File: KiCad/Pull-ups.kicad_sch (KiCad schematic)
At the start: 21 parts

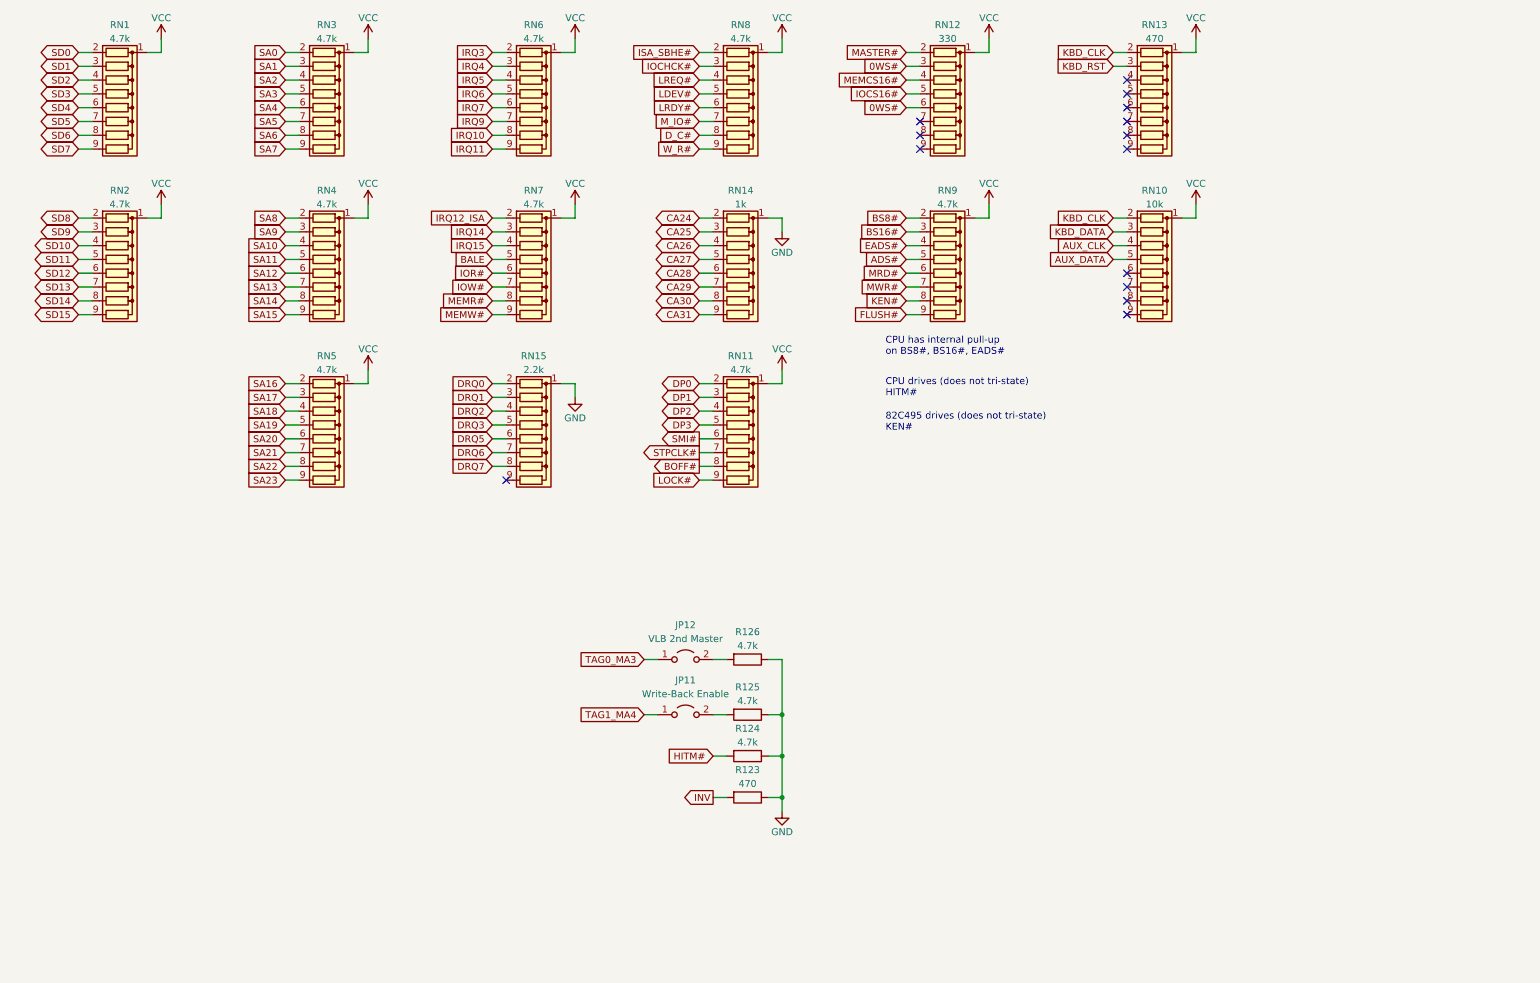
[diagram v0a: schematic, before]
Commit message: Version 0.3: Update DRAM schematic, pull-ups/pull-downs, CPU configuration jumpers
Signed-off-by: Sergey Kiselev <skiselev@gmail.com>
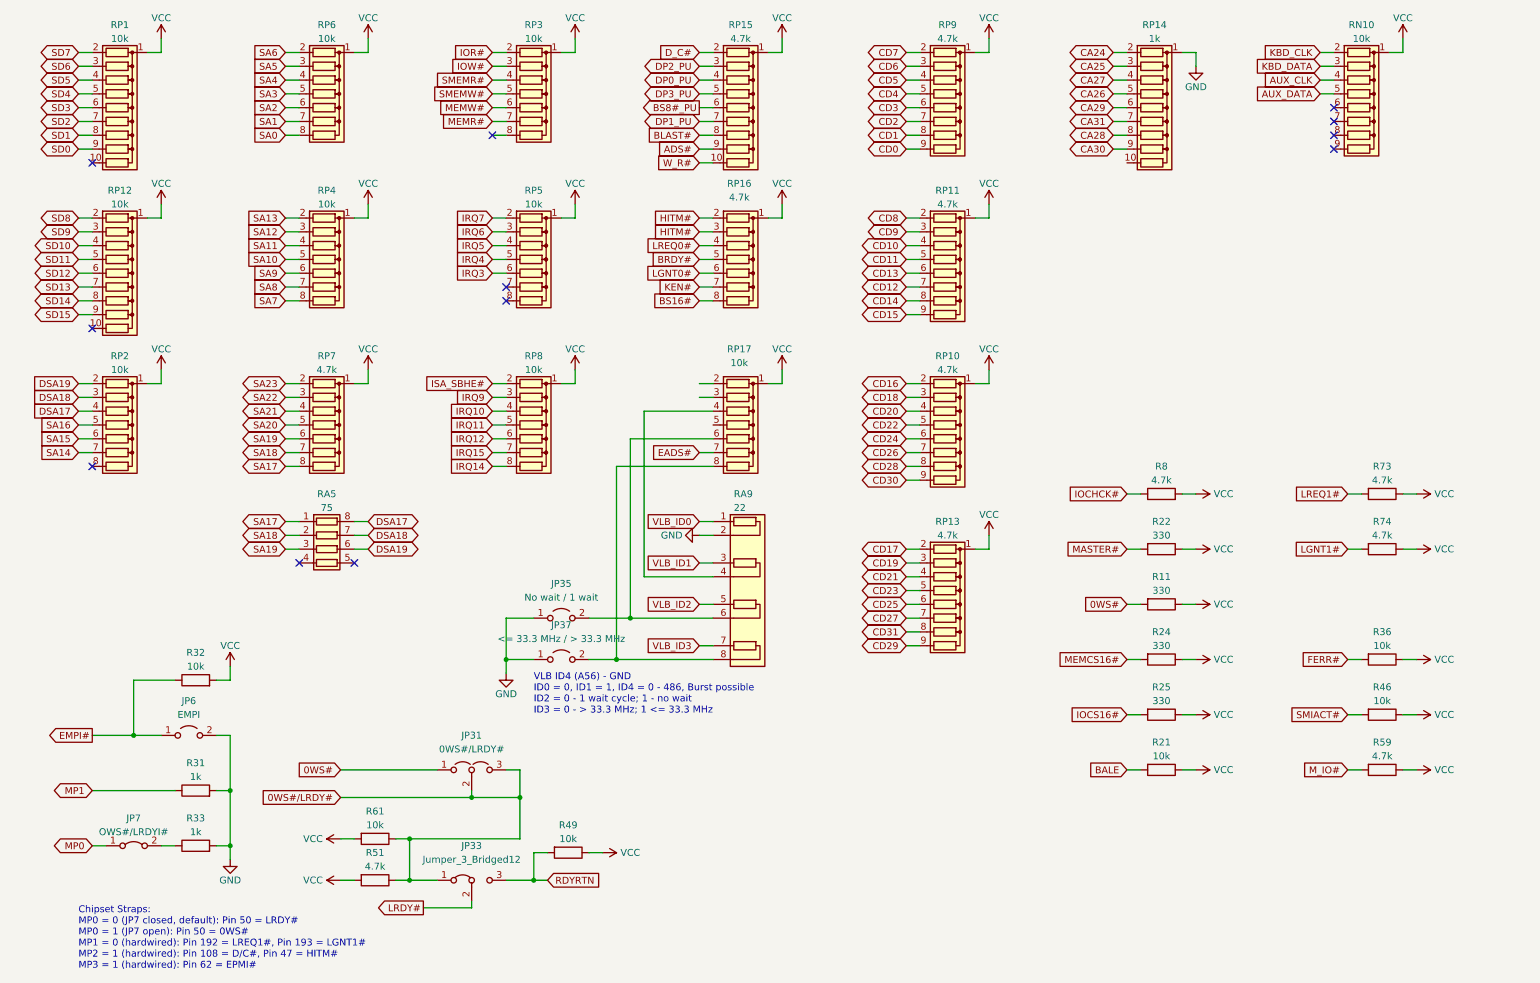
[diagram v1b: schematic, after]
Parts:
- removed JP11: Write-Back Enable, symbol Jumper:Jumper_2_Open
- removed JP12: VLB 2nd Master, symbol Jumper:Jumper_2_Open
- removed R123: 470, symbol Device:R
- removed R124, R125, R126: 4.7k, symbol Device:R
- removed RN1, RN11, RN2, RN3, RN4, RN5, RN6, RN7, RN8, RN9: 4.7k, Resistor_THT:R_Array_SIP9, symbol Device:R_Network08
- removed RN12: 330, Resistor_THT:R_Array_SIP9, symbol Device:R_Network08
- removed RN13: 470, Resistor_THT:R_Array_SIP9, symbol Device:R_Network08
- removed RN14: 1k, Resistor_THT:R_Array_SIP9, symbol Device:R_Network08
- removed RN15: 2.2k, Resistor_THT:R_Array_SIP9, symbol Device:R_Network08
- added JP31: 0WS#/LRDY#, symbol Jumper:Jumper_3_Open
- added JP33: Jumper_3_Bridged12, symbol Jumper:Jumper_3_Bridged12
- added JP35: No wait / 1 wait, symbol Jumper:Jumper_2_Open
- added JP37: <= 33.3 MHz / > 33.3 MHz, symbol Jumper:Jumper_2_Open
- added JP6: EMPI, symbol Jumper:Jumper_2_Open
- added JP7: OWS#/LRDYI#, symbol Jumper:Jumper_2_Bridged
- added R11, R22, R24, R25: 330, symbol Device:R
- added R21, R32, R36, R46, R49, R61: 10k, symbol Device:R
- added R31, R33: 1k, symbol Device:R
- added R51, R59, R73, R74, R8: 4.7k, symbol Device:R
- added RA5: 75, symbol Device:R_Pack04
- added RA9: 22, Resistor_THT:R_Array_SIP8, symbol Device:R_Pack04_SIP
- added RP1, RP12: 10k, Resistor_THT:R_Array_SIP10, symbol Device:R_Network09
- added RP10, RP11, RP13, RP9: 4.7k, Resistor_THT:R_Array_SIP9, symbol Device:R_Network08
- added RP14: 1k, Resistor_THT:R_Array_SIP10, symbol Device:R_Network09
- added RP15: 4.7k, Resistor_THT:R_Array_SIP10, symbol Device:R_Network09
- added RP16, RP7: 4.7k, Resistor_THT:R_Array_SIP8, symbol Device:R_Network07
- added RP17, RP2, RP3, RP4, RP5, RP6, RP8: 10k, Resistor_THT:R_Array_SIP8, symbol Device:R_Network07
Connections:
- net 0WS#: now also JP31.1 (A), R11.2
- net ADS#: now also RP15.9 (R8)
- net BALE: now also R21.2
- net BS16#: now also RP16.8 (R7)
- net CA24: now also RP14.2 (R1)
- net CA25: now also RP14.3 (R2)
- net CA26: now also RP14.5 (R4)
- net CA27: now also RP14.4 (R3)
- net CA28: now also RP14.8 (R7)
- net CA29: now also RP14.6 (R5)
- net CA30: now also RP14.9 (R8)
- net CA31: now also RP14.7 (R6)
- net D_C#: now also RP15.2 (R1)
- net EADS#: now also RP17.7 (R6)
- net GND: now also JP35.1 (A), JP37.1 (A), JP6.2 (B), R31.2, R33.2, RA9.2 (R1.2), RP14.1 (common)
- net HITM#: now also RP16.2 (R1), RP16.3 (R2)
- net IOCHCK#: now also R8.1
- net IOCS16#: now also R25.2
- net IOR#: now also RP3.2 (R1)
- net IOW#: now also RP3.3 (R2)
- net IRQ10: now also RP8.4 (R3)
- net IRQ11: now also RP8.5 (R4)
- net IRQ14: now also RP8.8 (R7)
- net IRQ15: now also RP8.7 (R6)
- net IRQ3: now also RP5.6 (R5)
- net IRQ4: now also RP5.5 (R4)
- net IRQ5: now also RP5.4 (R3)
- net IRQ6: now also RP5.3 (R2)
- net IRQ7: now also RP5.2 (R1)
- net IRQ9: now also RP8.3 (R2)
- net ISA_SBHE#: now also RP8.2 (R1)
- net KEN#: now also RP16.7 (R6)
- net LRDY#: now also JP33.2 (C)
- net MASTER#: now also R22.2
- net MEMCS16#: now also R24.2
- net MEMR#: now also RP3.7 (R6)
- net MEMW#: now also RP3.6 (R5)
- net M_IO#: now also R59.2
- net SA0: now also RP6.8 (R7)
- net SA1: now also RP6.7 (R6)
- net SA10: now also RP4.5 (R4)
- net SA11: now also RP4.4 (R3)
- net SA12: now also RP4.3 (R2)
- net SA13: now also RP4.2 (R1)
- net SA14: now also RP2.7 (R6)
- net SA15: now also RP2.6 (R5)
- net SA16: now also RP2.5 (R4)
- net SA17: now also RA5.1 (R1.1), RP7.8 (R7)
- net SA18: now also RA5.2 (R2.1), RP7.7 (R6)
- net SA19: now also RA5.3 (R3.1), RP7.6 (R5)
- net SA2: now also RP6.6 (R5)
- net SA20: now also RP7.5 (R4)
- net SA21: now also RP7.4 (R3)
- net SA22: now also RP7.3 (R2)
- net SA23: now also RP7.2 (R1)
- net SA3: now also RP6.5 (R4)
- net SA4: now also RP6.4 (R3)
- net SA5: now also RP6.3 (R2)
- net SA6: now also RP6.2 (R1)
- net SA7: now also RP4.8 (R7)
- net SA8: now also RP4.7 (R6)
- net SA9: now also RP4.6 (R5)
- net SD0: now also RP1.9 (R8)
- net SD1: now also RP1.8 (R7)
- net SD10: now also RP12.4 (R3)
- net SD11: now also RP12.5 (R4)
- net SD12: now also RP12.6 (R5)
- net SD13: now also RP12.7 (R6)
- net SD14: now also RP12.8 (R7)
- net SD15: now also RP12.9 (R8)
- net SD2: now also RP1.7 (R6)
- net SD3: now also RP1.6 (R5)
- net SD4: now also RP1.5 (R4)
- net SD5: now also RP1.4 (R3)
- net SD6: now also RP1.3 (R2)
- net SD7: now also RP1.2 (R1)
- net SD8: now also RP12.2 (R1)
- net SD9: now also RP12.3 (R2)
- net VCC: now also R11.1, R21.1, R22.1, R24.1, R25.1, R32.2, R36.1, R46.1, R49.1, R51.2, R59.1, R61.2, R73.1, R74.1, R8.2, RP1.1 (common), RP10.1 (common), RP11.1 (common), RP12.1 (common), RP13.1 (common), RP15.1 (common), RP16.1 (common), RP17.1 (common), RP2.1 (common), RP3.1 (common), RP4.1 (common), RP5.1 (common), RP6.1 (common), RP7.1 (common), RP8.1 (common), RP9.1 (common)
- net W_R#: now also RP15.10 (R9)
- new net: RA9.4 (R2.2), RP17.4 (R3)
- new net: JP35.2 (B), RA9.6 (R3.2), RP17.6 (R5)
- new net: JP37.2 (B), RA9.8 (R4.2), RP17.8 (R7)
- new net: JP7.2 (B), R33.1
- new net 0WS#/LRDY#: JP31.2 (C), JP31.3 (B), JP33.1 (A), R51.1, R61.1
- new net BLAST#: RP15.8 (R7)
- new net BRDY#: RP16.5 (R4)
- new net BS8#_PU: RP15.6 (R5)
- new net CD0: RP9.9 (R8)
- new net CD1: RP9.8 (R7)
- new net CD10: RP11.4 (R3)
- new net CD11: RP11.5 (R4)
- new net CD12: RP11.7 (R6)
- new net CD13: RP11.6 (R5)
- new net CD14: RP11.8 (R7)
- new net CD15: RP11.9 (R8)
- new net CD16: RP10.2 (R1)
- new net CD17: RP13.2 (R1)
- new net CD18: RP10.3 (R2)
- new net CD19: RP13.3 (R2)
- new net CD2: RP9.7 (R6)
- new net CD20: RP10.4 (R3)
- new net CD21: RP13.4 (R3)
- new net CD22: RP10.5 (R4)
- new net CD23: RP13.5 (R4)
- new net CD24: RP10.6 (R5)
- new net CD25: RP13.6 (R5)
- new net CD26: RP10.7 (R6)
- new net CD27: RP13.7 (R6)
- new net CD28: RP10.8 (R7)
- new net CD29: RP13.9 (R8)
- new net CD3: RP9.6 (R5)
- new net CD30: RP10.9 (R8)
- new net CD31: RP13.8 (R7)
- new net CD4: RP9.5 (R4)
- new net CD5: RP9.4 (R3)
- new net CD6: RP9.3 (R2)
- new net CD7: RP9.2 (R1)
- new net CD8: RP11.2 (R1)
- new net CD9: RP11.3 (R2)
- new net DP0_PU: RP15.4 (R3)
- new net DP1_PU: RP15.7 (R6)
- new net DP2_PU: RP15.3 (R2)
- new net DP3_PU: RP15.5 (R4)
- new net DSA17: RA5.8 (R1.2), RP2.4 (R3)
- new net DSA18: RA5.7 (R2.2), RP2.3 (R2)
- new net DSA19: RA5.6 (R3.2), RP2.2 (R1)
- new net EMPI#: JP6.1 (A), R32.1
- new net FERR#: R36.2
- new net IRQ12: RP8.6 (R5)
- new net LGNT0#: RP16.6 (R5)
- new net LGNT1#: R74.2
- new net LREQ0#: RP16.4 (R3)
- new net LREQ1#: R73.2
- new net MP0: JP7.1 (A)
- new net MP1: R31.1
- new net RDYRTN: JP33.3 (B), R49.2
- new net SMEMR#: RP3.4 (R3)
- new net SMEMW#: RP3.5 (R4)
- new net SMIACT#: R46.2
- new net VLB_ID0: RA9.1 (R1.1)
- new net VLB_ID1: RA9.3 (R2.1)
- new net VLB_ID2: RA9.5 (R3.1)
- new net VLB_ID3: RA9.7 (R4.1)
- no-connect marks 14 -> 12
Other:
- note added: "Chipset Straps: MP0 = 0 (JP7 closed, default): Pin 50 = LRDY# MP0 = 1 (JP7 open): Pin 50 = 0WS# MP1 = 0 (hardwired): Pin 192 = LREQ1#, Pin 193 = LGNT1# MP2 = 1 (hardwired): Pin 108 = D/C#, Pin 47 = HITM# MP3 = 1 (hardwired): Pin 62 = EPMI#"
- note added: "VLB ID4 (A56) - GND ID0 = 0, ID1 = 1, ID4 = 0 - 486, Burst possible ID2 = 0 - 1 wait cycle; 1 - no wait ID3 = 0 - > 33.3 MHz; 1 <= 33.3 MHz"
- note removed: "82C495 drives (does not tri-state) KEN#"
- note removed: "CPU drives (does not tri-state) HITM#"
- note removed: "CPU has internal pull-up on BS8#, BS16#, EADS#"
- moved on the sheet: RN10

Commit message: Version 0.4: Update chipset connection
Signed-off-by: Sergey Kiselev <skiselev@gmail.com>
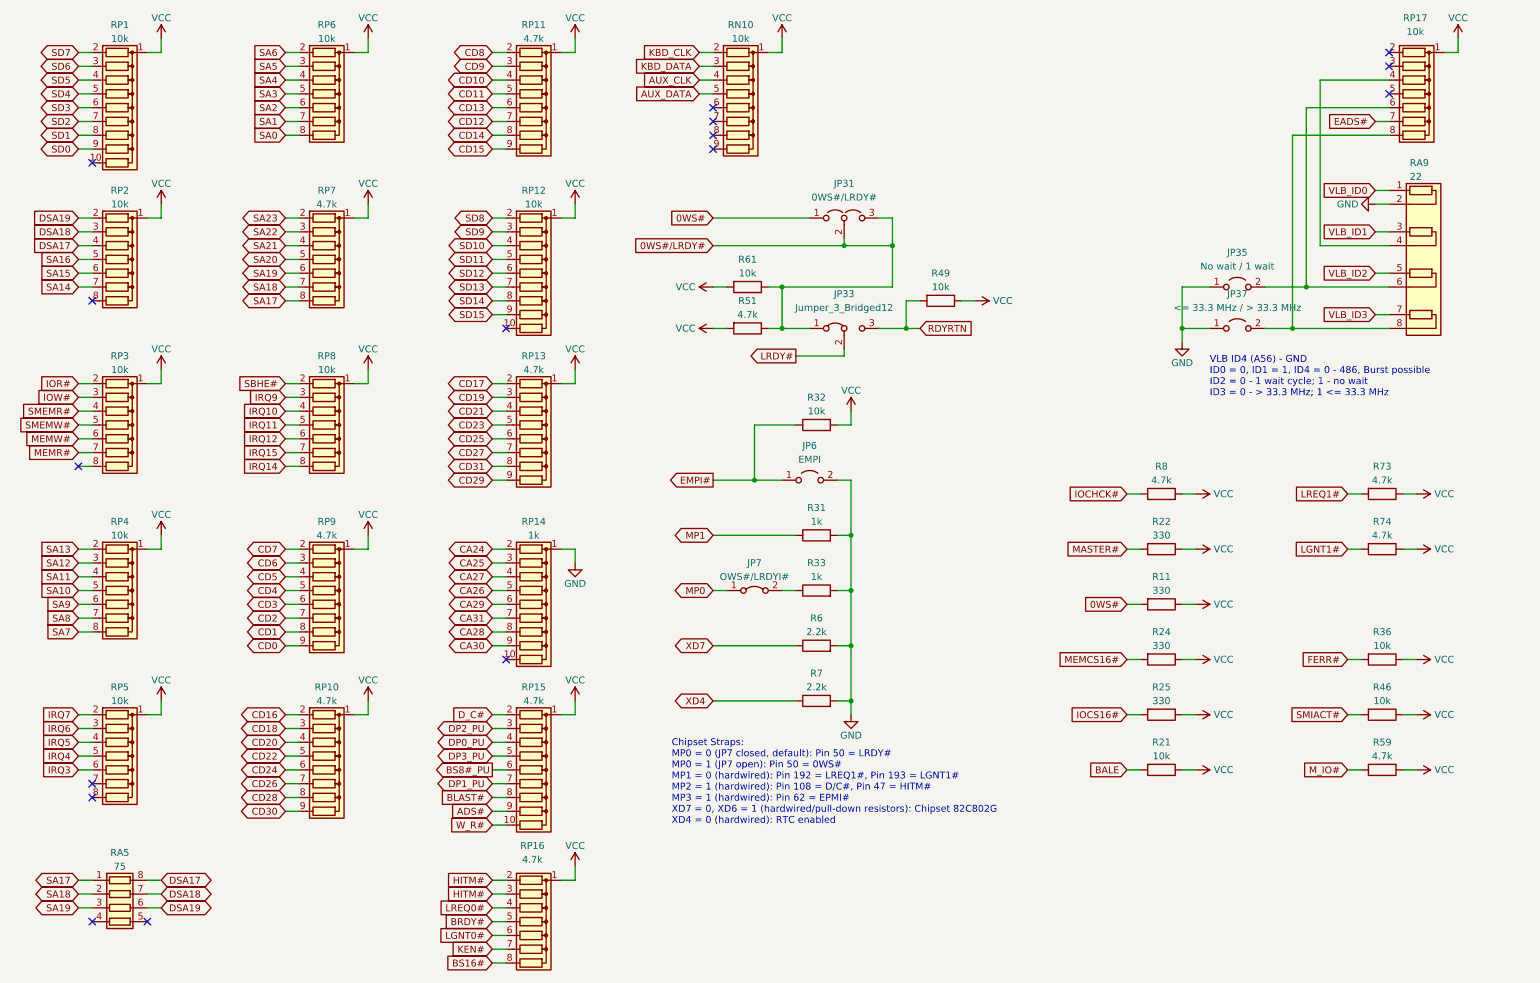
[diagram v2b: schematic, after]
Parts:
- added R6, R7: 2.2k, Resistor_SMD:R_0612_1632Metric_Pad1.18x3.40mm_HandSolder, symbol Device:R
- JP31, JP33: footprint (none) -> My_Components:Conn_Pin_Header_3x1_2.54mm
- JP35, JP37, JP6, JP7: footprint (none) -> My_Components:Conn_Pin_Header_2x1_2.54mm
- R11, R21, R22, R24, R25, R31, R32, R33, R36, R46, R49, R51, R59, R61, R73, R74, R8: footprint (none) -> Resistor_SMD:R_0612_1632Metric_Pad1.18x3.40mm_HandSolder
- RA5: footprint (none) -> Resistor_THT:R_Array_SIP8
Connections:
- net GND: now also R6.2, R7.2
- net ISA_SBHE# renamed SBHE#
- new net XD4: R7.1
- new net XD7: R6.1
- no-connect marks 12 -> 16
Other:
- note added: "Chipset Straps: MP0 = 0 (JP7 closed, default): Pin 50 = LRDY# MP0 = 1 (JP7 open): Pin 50 = 0WS# MP1 = 0 (hardwired): Pin 192 = LREQ1#, Pin 193 = LGNT1# MP2 = 1 (hardwired): Pin 108 = D/C#, Pin 47 = HITM# MP3 = 1 (hardwired): Pin 62 = EPMI# XD7 = 0, XD6 = 1 (hardwired/pull-down resistors): Chipset 82C802G XD4 = 0 (hardwired): RTC enabled"
- note removed: "Chipset Straps: MP0 = 0 (JP7 closed, default): Pin 50 = LRDY# MP0 = 1 (JP7 open): Pin 50 = 0WS# MP1 = 0 (hardwired): Pin 192 = LREQ1#, Pin 193 = LGNT1# MP2 = 1 (hardwired): Pin 108 = D/C#, Pin 47 = HITM# MP3 = 1 (hardwired): Pin 62 = EPMI#"
- moved on the sheet: JP31, JP33, JP35, JP37, JP6, JP7, R31, R32, R33, R49, R51, R61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
